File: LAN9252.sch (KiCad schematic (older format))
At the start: 47 parts, among them U1 LAN9252, U2 24LC00, Y1 Crystal_GND24

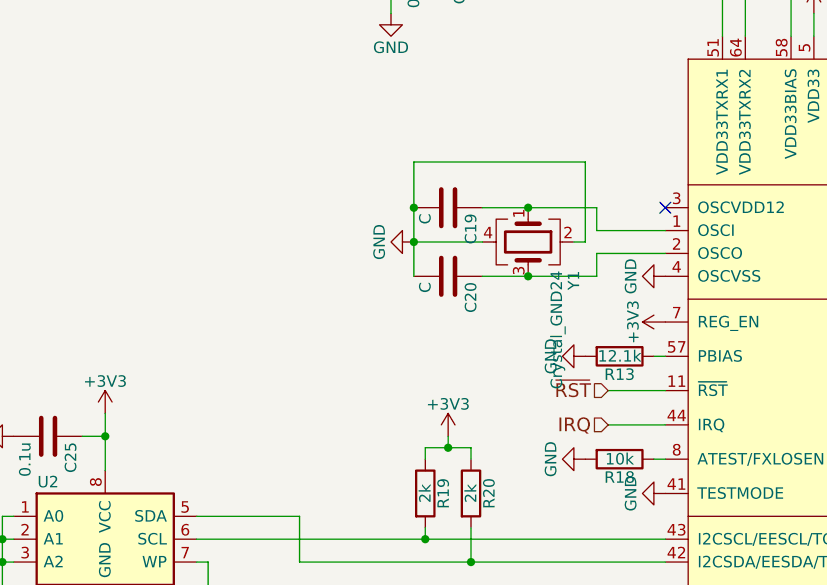
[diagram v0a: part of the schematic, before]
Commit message: 外形線を変更
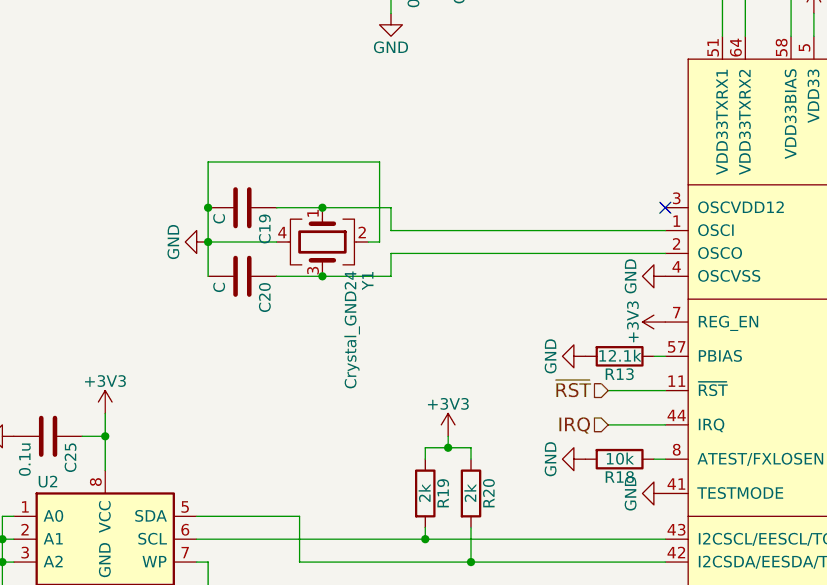
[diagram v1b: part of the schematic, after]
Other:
- moved on the sheet: C19, C20, Y1
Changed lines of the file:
@@
 L C C19
 U 1 1 58DB294F
-P 3650 3850
-F 0 "C19" H 3675 3950 50  0000 L CNN
-F 1 "C" H 3675 3750 50  0000 L CNN
-F 2 "Capacitors_SMD:C_0603" H 3688 3700 50  0001 C CNN
-F 3 "" H 3650 3850 50  0000 C CNN
-	1    3650 3850
+P 2750 3850
+F 0 "C19" H 2775 3950 50  0000 L CNN
+F 1 "C" H 2775 3750 50  0000 L CNN
+F 2 "Capacitors_SMD:C_0603" H 2788 3700 50  0001 C CNN
+F 3 "" H 2750 3850 50  0000 C CNN
+	1    2750 3850
 	0    1    1    0
 $EndComp
@@
 L C C20
 U 1 1 58DB2B1B
-P 3650 4150
-F 0 "C20" H 3675 4250 50  0000 L CNN
-F 1 "C" H 3675 4050 50  0000 L CNN
-F 2 "Capacitors_SMD:C_0603" H 3688 4000 50  0001 C CNN
-F 3 "" H 3650 4150 50  0000 C CNN
-	1    3650 4150
+P 2750 4150
+F 0 "C20" H 2775 4250 50  0000 L CNN
+F 1 "C" H 2775 4050 50  0000 L CNN
+F 2 "Capacitors_SMD:C_0603" H 2788 4000 50  0001 C CNN
+F 3 "" H 2750 4150 50  0000 C CNN
+	1    2750 4150
 	0    1    1    0
 $EndComp
@@
 L GND #PWR055
 U 1 1 58DB2B81
-P 3500 4000
-F 0 "#PWR055" H 3500 3750 50  0001 C CNN
-F 1 "GND" H 3500 3850 50  0000 C CNN
-F 2 "" H 3500 4000 50  0000 C CNN
-F 3 "" H 3500 4000 50  0000 C CNN
-	1    3500 4000
+P 2600 4000
+F 0 "#PWR055" H 2600 3750 50  0001 C CNN
+F 1 "GND" H 2600 3850 50  0000 C CNN
+F 2 "" H 2600 4000 50  0000 C CNN
+F 3 "" H 2600 4000 50  0000 C CNN
+	1    2600 4000
 	0    1    1    0
 $EndComp
@@
 Connection ~ 7150 3450
 Wire Wire Line
-	3500 3650 3500 4150
-Connection ~ 3500 4000
-Wire Wire Line
-	3800 4150 4300 4150
-Wire Wire Line
-	3800 3850 4300 3850
-Wire Wire Line
-	4600 3950 4300 3950
-Wire Wire Line
-	4300 3950 4300 3850
-Connection ~ 4000 3850
-Wire Wire Line
-	4600 4050 4300 4050
-Wire Wire Line
-	4300 4050 4300 4150
-Connection ~ 4000 4150
+	2600 3650 2600 4150
+Connection ~ 2600 4000
+Wire Wire Line
+	2900 4150 3400 4150
+Wire Wire Line
+	2900 3850 3400 3850
+Wire Wire Line
+	3400 3950 4600 3950
+Wire Wire Line
+	3400 3850 3400 3950
+Connection ~ 3100 3850
+Wire Wire Line
+	3400 4050 4600 4050
+Wire Wire Line
+	3400 4050 3400 4150
+Connection ~ 3100 4150
 Wire Wire Line
 	3350 1600 3350 2600
@@
 L Crystal_GND24 Y1
 U 1 1 58DA8433
-P 4000 4000
-F 0 "Y1" H 4125 4200 50  0000 L CNN
-F 1 "Crystal_GND24" H 4125 4125 50  0000 L CNN
-F 2 "Crystals:Crystal_SMD_Abracon_ABM8G-4pin_3.2x2.5mm" H 4000 4000 50  0001 C CNN
-F 3 "" H 4000 4000 50  0001 C CNN
-	1    4000 4000
-	0    1    1    0
-$EndComp
-Wire Wire Line
-	3800 4000 3500 4000
-Wire Wire Line
-	4200 4000 4250 4000
-Wire Wire Line
-	4250 4000 4250 3650
-Wire Wire Line
-	4250 3650 3500 3650
-Connection ~ 3500 3850
+P 3100 4000
+F 0 "Y1" H 3225 4200 50  0000 L CNN
+F 1 "Crystal_GND24" H 3225 4125 50  0000 L CNN
+F 2 "Crystals:Crystal_SMD_Abracon_ABM8G-4pin_3.2x2.5mm" H 3100 4000 50  0001 C CNN
+F 3 "" H 3100 4000 50  0001 C CNN
+	1    3100 4000
+	0    1    1    0
+$EndComp
+Wire Wire Line
+	2900 4000 2600 4000
+Wire Wire Line
+	3300 4000 3350 4000
+Wire Wire Line
+	3350 4000 3350 3650
+Wire Wire Line
+	3350 3650 2600 3650
+Connection ~ 2600 3850
 $Comp
 L LAN9252 U1

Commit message: CHS GNDとPCB GNDを抵抗で接続
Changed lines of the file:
@@
 $EndDescr
 $Comp
-L GND #PWR046
+L GND #PWR050
 U 1 1 58D8F4AE
 P 6400 6000
-F 0 "#PWR046" H 6400 5750 50  0001 C CNN
+F 0 "#PWR050" H 6400 5750 50  0001 C CNN
 F 1 "GND" H 6400 5850 50  0000 C CNN
 F 2 "" H 6400 6000 50  0000 C CNN
@@
 NoConn ~ 4600 3850
 $Comp
-L GND #PWR047
+L GND #PWR051
 U 1 1 58D8FBF8
 P 4600 4150
-F 0 "#PWR047" H 4600 3900 50  0001 C CNN
+F 0 "#PWR051" H 4600 3900 50  0001 C CNN
 F 1 "GND" H 4600 4000 50  0000 C CNN
 F 2 "" H 4600 4150 50  0000 C CNN
@@
 $EndComp
 $Comp
-L GND #PWR048
+L GND #PWR052
 U 1 1 58D8FC8D
 P 4250 4500
-F 0 "#PWR048" H 4250 4250 50  0001 C CNN
+F 0 "#PWR052" H 4250 4250 50  0001 C CNN
 F 1 "GND" H 4250 4350 50  0000 C CNN
 F 2 "" H 4250 4500 50  0000 C CNN
@@
 $EndComp
 $Comp
-L GND #PWR049
+L GND #PWR053
 U 1 1 58D8FD81
 P 4600 5100
-F 0 "#PWR049" H 4600 4850 50  0001 C CNN
+F 0 "#PWR053" H 4600 4850 50  0001 C CNN
 F 1 "GND" H 4600 4950 50  0000 C CNN
 F 2 "" H 4600 5100 50  0000 C CNN
@@
 $EndComp
 $Comp
-L GND #PWR050
+L GND #PWR054
 U 1 1 58D8CF70
 P 7000 3900
-F 0 "#PWR050" H 7000 3650 50  0001 C CNN
+F 0 "#PWR054" H 7000 3650 50  0001 C CNN
 F 1 "GND" H 7000 3750 50  0000 C CNN
 F 2 "" H 7000 3900 50  0000 C CNN
@@
 $EndComp
 $Comp
-L GND #PWR051
+L GND #PWR055
 U 1 1 58D8D10E
 P 7000 5350
-F 0 "#PWR051" H 7000 5100 50  0001 C CNN
+F 0 "#PWR055" H 7000 5100 50  0001 C CNN
 F 1 "GND" H 7000 5200 50  0000 C CNN
 F 2 "" H 7000 5350 50  0000 C CNN
@@
 $EndComp
 $Comp
-L GND #PWR052
+L GND #PWR056
 U 1 1 58D8D588
 P 8150 4700
-F 0 "#PWR052" H 8150 4450 50  0001 C CNN
+F 0 "#PWR056" H 8150 4450 50  0001 C CNN
 F 1 "GND" H 8150 4550 50  0000 C CNN
 F 2 "" H 8150 4700 50  0000 C CNN
@@
 $EndComp
 $Comp
-L GND #PWR053
+L GND #PWR057
 U 1 1 58D8F32E
 P 9350 5550
-F 0 "#PWR053" H 9350 5300 50  0001 C CNN
+F 0 "#PWR057" H 9350 5300 50  0001 C CNN
 F 1 "GND" H 9350 5400 50  0000 C CNN
 F 2 "" H 9350 5550 50  0000 C CNN
@@
 $EndComp
 $Comp
-L GND #PWR054
+L GND #PWR058
 U 1 1 58DAEFCA
 P 7200 3450
-F 0 "#PWR054" H 7200 3200 50  0001 C CNN
+F 0 "#PWR058" H 7200 3200 50  0001 C CNN
 F 1 "GND" H 7200 3300 50  0000 C CNN
 F 2 "" H 7200 3450 50  0000 C CNN
@@
 $EndComp
 $Comp
-L GND #PWR055
+L GND #PWR059
 U 1 1 58DB2B81
 P 2600 4000
-F 0 "#PWR055" H 2600 3750 50  0001 C CNN
+F 0 "#PWR059" H 2600 3750 50  0001 C CNN
 F 1 "GND" H 2600 3850 50  0000 C CNN
 F 2 "" H 2600 4000 50  0000 C CNN
@@
 $EndComp
 $Comp
-L +3V3 #PWR056
+L +3V3 #PWR060
 U 1 1 58DB404A
 P 3350 1600
-F 0 "#PWR056" H 3350 1450 50  0001 C CNN
+F 0 "#PWR060" H 3350 1450 50  0001 C CNN
 F 1 "+3V3" H 3350 1740 50  0000 C CNN
 F 2 "" H 3350 1600 50  0000 C CNN
@@
 $EndComp
 $Comp
-L GND #PWR057
+L GND #PWR061
 U 1 1 58DBACA0
 P 3400 3000
-F 0 "#PWR057" H 3400 2750 50  0001 C CNN
+F 0 "#PWR061" H 3400 2750 50  0001 C CNN
 F 1 "GND" H 3400 2850 50  0000 C CNN
 F 2 "" H 3400 3000 50  0000 C CNN
@@
 $EndComp
 $Comp
-L +3V3 #PWR058
+L +3V3 #PWR062
 U 1 1 58DBB1A4
 P 5250 3000
-F 0 "#PWR058" H 5250 2850 50  0001 C CNN
+F 0 "#PWR062" H 5250 2850 50  0001 C CNN
 F 1 "+3V3" H 5250 3140 50  0000 C CNN
 F 2 "" H 5250 3000 50  0000 C CNN
@@
 $EndComp
 $Comp
-L +3V3 #PWR059
+L +3V3 #PWR063
 U 1 1 58DBB719
 P 5600 3000
-F 0 "#PWR059" H 5600 2850 50  0001 C CNN
+F 0 "#PWR063" H 5600 2850 50  0001 C CNN
 F 1 "+3V3" H 5600 3140 50  0000 C CNN
 F 2 "" H 5600 3000 50  0000 C CNN
@@
 $EndComp
 $Comp
-L +3V3 #PWR060
+L +3V3 #PWR064
 U 1 1 58DBBE53
 P 4600 4350
-F 0 "#PWR060" H 4600 4200 50  0001 C CNN
+F 0 "#PWR064" H 4600 4200 50  0001 C CNN
 F 1 "+3V3" H 4600 4490 50  0000 C CNN
 F 2 "" H 4600 4350 50  0000 C CNN
@@
 $EndComp
 $Comp
-L GND #PWR061
+L GND #PWR065
 U 1 1 58DBE707
 P 7250 2800
-F 0 "#PWR061" H 7250 2550 50  0001 C CNN
+F 0 "#PWR065" H 7250 2550 50  0001 C CNN
 F 1 "GND" H 7250 2650 50  0000 C CNN
 F 2 "" H 7250 2800 50  0000 C CNN
@@
 $EndComp
 $Comp
-L GND #PWR062
+L GND #PWR066
 U 1 1 58DC454A
 P 2300 2450
-F 0 "#PWR062" H 2300 2200 50  0001 C CNN
+F 0 "#PWR066" H 2300 2200 50  0001 C CNN
 F 1 "GND" H 2300 2300 50  0000 C CNN
 F 2 "" H 2300 2450 50  0000 C CNN
@@
 $EndComp
 $Comp
-L +3V3 #PWR063
+L +3V3 #PWR067
 U 1 1 58DC4AF2
 P 2300 1950
-F 0 "#PWR063" H 2300 1800 50  0001 C CNN
+F 0 "#PWR067" H 2300 1800 50  0001 C CNN
 F 1 "+3V3" H 2300 2090 50  0000 C CNN
 F 2 "" H 2300 1950 50  0000 C CNN
@@
 $EndComp
 $Comp
-L GND #PWR064
+L GND #PWR068
 U 1 1 58DD07AD
 P 4250 4950
-F 0 "#PWR064" H 4250 4700 50  0001 C CNN
+F 0 "#PWR068" H 4250 4700 50  0001 C CNN
 F 1 "GND" H 4250 4800 50  0000 C CNN
 F 2 "" H 4250 4950 50  0000 C CNN
@@
 $EndComp
 $Comp
-L +3V3 #PWR065
+L +3V3 #PWR069
 U 1 1 58DD57EA
 P 3650 4850
-F 0 "#PWR065" H 3650 4700 50  0001 C CNN
+F 0 "#PWR069" H 3650 4700 50  0001 C CNN
 F 1 "+3V3" H 3650 4990 50  0000 C CNN
 F 2 "" H 3650 4850 50  0000 C CNN
@@
 	3400 4050 4600 4050
 Wire Wire Line
-	3400 4050 3400 4150
+	3400 4150 3400 4050
 Connection ~ 3100 4150
 Wire Wire Line
@@
 	3000 5200 3000 5400
 $Comp
-L GND #PWR066
+L GND #PWR070
 U 1 1 58E26D3D
 P 2150 5600
-F 0 "#PWR066" H 2150 5350 50  0001 C CNN
+F 0 "#PWR070" H 2150 5350 50  0001 C CNN
 F 1 "GND" H 2150 5450 50  0000 C CNN
 F 2 "" H 2150 5600 50  0000 C CNN
@@
 Connection ~ 1700 5300
 $Comp
-L GND #PWR067
+L GND #PWR071
 U 1 1 58E27E20
 P 1700 5900
-F 0 "#PWR067" H 1700 5650 50  0001 C CNN
+F 0 "#PWR071" H 1700 5650 50  0001 C CNN
 F 1 "GND" H 1700 5750 50  0000 C CNN
 F 2 "" H 1700 5900 50  0000 C CNN
@@
 $EndComp
 $Comp
-L GND #PWR068
+L GND #PWR072
 U 1 1 58E29423
 P 1750 4850
-F 0 "#PWR068" H 1750 4600 50  0001 C CNN
+F 0 "#PWR072" H 1750 4600 50  0001 C CNN
 F 1 "GND" H 1750 4700 50  0000 C CNN
 F 2 "" H 1750 4850 50  0000 C CNN
@@
 $EndComp
 $Comp
-L +3V3 #PWR069
+L +3V3 #PWR073
 U 1 1 58E2970F
 P 2150 4750
-F 0 "#PWR069" H 2150 4600 50  0001 C CNN
+F 0 "#PWR073" H 2150 4600 50  0001 C CNN
 F 1 "+3V3" H 2150 4890 50  0000 C CNN
 F 2 "" H 2150 4750 50  0000 C CNN

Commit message: 抵抗とかコンデンサを追加
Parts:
- added C32, C33: 10u, Capacitors_SMD:C_0805, symbol C
- added R42, R43, R44: 10k, Resistors_SMD:R_0603, symbol R
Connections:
- net +3V3: now also C32.1, C33.1, R42.1
- net GND: now also C32.2, C33.2, R43.2, R44.2
- net LINKACTLED0: now also R43.1
- net LINKACTLED1: now also R44.1
- net RUNLED: now also R42.2
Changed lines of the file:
@@
 $EndDescr
 $Comp
-L GND #PWR050
+L GND #PWR054
 U 1 1 58D8F4AE
 P 6400 6000
-F 0 "#PWR050" H 6400 5750 50  0001 C CNN
+F 0 "#PWR054" H 6400 5750 50  0001 C CNN
 F 1 "GND" H 6400 5850 50  0000 C CNN
 F 2 "" H 6400 6000 50  0000 C CNN
@@
 NoConn ~ 4600 3850
 $Comp
-L GND #PWR051
+L GND #PWR055
 U 1 1 58D8FBF8
 P 4600 4150
-F 0 "#PWR051" H 4600 3900 50  0001 C CNN
+F 0 "#PWR055" H 4600 3900 50  0001 C CNN
 F 1 "GND" H 4600 4000 50  0000 C CNN
 F 2 "" H 4600 4150 50  0000 C CNN
@@
 $EndComp
 $Comp
-L GND #PWR052
+L GND #PWR056
 U 1 1 58D8FC8D
 P 4250 4500
-F 0 "#PWR052" H 4250 4250 50  0001 C CNN
+F 0 "#PWR056" H 4250 4250 50  0001 C CNN
 F 1 "GND" H 4250 4350 50  0000 C CNN
 F 2 "" H 4250 4500 50  0000 C CNN
@@
 $EndComp
 $Comp
-L GND #PWR053
+L GND #PWR057
 U 1 1 58D8FD81
 P 4600 5100
-F 0 "#PWR053" H 4600 4850 50  0001 C CNN
+F 0 "#PWR057" H 4600 4850 50  0001 C CNN
 F 1 "GND" H 4600 4950 50  0000 C CNN
 F 2 "" H 4600 5100 50  0000 C CNN
@@
 $EndComp
 $Comp
-L GND #PWR054
+L GND #PWR058
 U 1 1 58D8CF70
 P 7000 3900
-F 0 "#PWR054" H 7000 3650 50  0001 C CNN
+F 0 "#PWR058" H 7000 3650 50  0001 C CNN
 F 1 "GND" H 7000 3750 50  0000 C CNN
 F 2 "" H 7000 3900 50  0000 C CNN
@@
 $EndComp
 $Comp
-L GND #PWR055
+L GND #PWR059
 U 1 1 58D8D10E
 P 7000 5350
-F 0 "#PWR055" H 7000 5100 50  0001 C CNN
+F 0 "#PWR059" H 7000 5100 50  0001 C CNN
 F 1 "GND" H 7000 5200 50  0000 C CNN
 F 2 "" H 7000 5350 50  0000 C CNN
@@
 $EndComp
 $Comp
-L GND #PWR056
+L GND #PWR060
 U 1 1 58D8D588
 P 8150 4700
-F 0 "#PWR056" H 8150 4450 50  0001 C CNN
+F 0 "#PWR060" H 8150 4450 50  0001 C CNN
 F 1 "GND" H 8150 4550 50  0000 C CNN
 F 2 "" H 8150 4700 50  0000 C CNN
@@
 $EndComp
 $Comp
-L GND #PWR057
+L GND #PWR061
 U 1 1 58D8F32E
 P 9350 5550
-F 0 "#PWR057" H 9350 5300 50  0001 C CNN
+F 0 "#PWR061" H 9350 5300 50  0001 C CNN
 F 1 "GND" H 9350 5400 50  0000 C CNN
 F 2 "" H 9350 5550 50  0000 C CNN
@@
 Text HLabel 9150 4400 2    60   Input ~ 0
 VDDTXRX2
-Text HLabel 4350 5600 0    60   Input ~ 0
+Text HLabel 4050 5600 0    60   Input ~ 0
 LINKACTLED0
-Text HLabel 4350 5700 0    60   Input ~ 0
+Text HLabel 4050 5700 0    60   Input ~ 0
 LINKACTLED1
 $Comp
@@
 $EndComp
 $Comp
-L GND #PWR058
+L GND #PWR062
 U 1 1 58DAEFCA
 P 7200 3450
-F 0 "#PWR058" H 7200 3200 50  0001 C CNN
+F 0 "#PWR062" H 7200 3200 50  0001 C CNN
 F 1 "GND" H 7200 3300 50  0000 C CNN
 F 2 "" H 7200 3450 50  0000 C CNN
@@
 $EndComp
 $Comp
-L GND #PWR059
+L GND #PWR063
 U 1 1 58DB2B81
 P 2600 4000
-F 0 "#PWR059" H 2600 3750 50  0001 C CNN
+F 0 "#PWR063" H 2600 3750 50  0001 C CNN
 F 1 "GND" H 2600 3850 50  0000 C CNN
 F 2 "" H 2600 4000 50  0000 C CNN
@@
 $EndComp
 $Comp
-L +3V3 #PWR060
+L +3V3 #PWR064
 U 1 1 58DB404A
 P 3350 1600
-F 0 "#PWR060" H 3350 1450 50  0001 C CNN
+F 0 "#PWR064" H 3350 1450 50  0001 C CNN
 F 1 "+3V3" H 3350 1740 50  0000 C CNN
 F 2 "" H 3350 1600 50  0000 C CNN
@@
 $EndComp
 $Comp
-L GND #PWR061
+L GND #PWR065
 U 1 1 58DBACA0
 P 3400 3000
-F 0 "#PWR061" H 3400 2750 50  0001 C CNN
+F 0 "#PWR065" H 3400 2750 50  0001 C CNN
 F 1 "GND" H 3400 2850 50  0000 C CNN
 F 2 "" H 3400 3000 50  0000 C CNN
@@
 $EndComp
 $Comp
-L +3V3 #PWR062
+L +3V3 #PWR066
 U 1 1 58DBB1A4
 P 5250 3000
-F 0 "#PWR062" H 5250 2850 50  0001 C CNN
+F 0 "#PWR066" H 5250 2850 50  0001 C CNN
 F 1 "+3V3" H 5250 3140 50  0000 C CNN
 F 2 "" H 5250 3000 50  0000 C CNN
@@
 $EndComp
 $Comp
-L +3V3 #PWR063
+L +3V3 #PWR067
 U 1 1 58DBB719
 P 5600 3000
-F 0 "#PWR063" H 5600 2850 50  0001 C CNN
+F 0 "#PWR067" H 5600 2850 50  0001 C CNN
 F 1 "+3V3" H 5600 3140 50  0000 C CNN
 F 2 "" H 5600 3000 50  0000 C CNN
@@
 $EndComp
 $Comp
-L +3V3 #PWR064
+L +3V3 #PWR068
 U 1 1 58DBBE53
 P 4600 4350
-F 0 "#PWR064" H 4600 4200 50  0001 C CNN
+F 0 "#PWR068" H 4600 4200 50  0001 C CNN
 F 1 "+3V3" H 4600 4490 50  0000 C CNN
 F 2 "" H 4600 4350 50  0000 C CNN
@@
 $EndComp
 $Comp
-L GND #PWR065
+L GND #PWR069
 U 1 1 58DBE707
 P 7250 2800
-F 0 "#PWR065" H 7250 2550 50  0001 C CNN
+F 0 "#PWR069" H 7250 2550 50  0001 C CNN
 F 1 "GND" H 7250 2650 50  0000 C CNN
 F 2 "" H 7250 2800 50  0000 C CNN
@@
 $EndComp
 $Comp
-L GND #PWR066
+L GND #PWR070
 U 1 1 58DC454A
 P 2300 2450
-F 0 "#PWR066" H 2300 2200 50  0001 C CNN
+F 0 "#PWR070" H 2300 2200 50  0001 C CNN
 F 1 "GND" H 2300 2300 50  0000 C CNN
 F 2 "" H 2300 2450 50  0000 C CNN
@@
 $EndComp
 $Comp
-L +3V3 #PWR067
+L +3V3 #PWR071
 U 1 1 58DC4AF2
 P 2300 1950
-F 0 "#PWR067" H 2300 1800 50  0001 C CNN
+F 0 "#PWR071" H 2300 1800 50  0001 C CNN
 F 1 "+3V3" H 2300 2090 50  0000 C CNN
 F 2 "" H 2300 1950 50  0000 C CNN
@@
 $EndComp
 $Comp
-L GND #PWR068
+L GND #PWR072
 U 1 1 58DD07AD
 P 4250 4950
-F 0 "#PWR068" H 4250 4700 50  0001 C CNN
+F 0 "#PWR072" H 4250 4700 50  0001 C CNN
 F 1 "GND" H 4250 4800 50  0000 C CNN
 F 2 "" H 4250 4950 50  0000 C CNN
@@
 $EndComp
 $Comp
-L +3V3 #PWR069
+L +3V3 #PWR073
 U 1 1 58DD57EA
 P 3650 4850
-F 0 "#PWR069" H 3650 4700 50  0001 C CNN
+F 0 "#PWR073" H 3650 4700 50  0001 C CNN
 F 1 "+3V3" H 3650 4990 50  0000 C CNN
 F 2 "" H 3650 4850 50  0000 C CNN
@@
 Connection ~ 6650 2350
 Wire Wire Line
-	1800 2050 1800 2000
-Wire Wire Line
-	1800 2000 2800 2000
+	1800 2000 1800 2050
+Wire Wire Line
+	1300 2000 2800 2000
 Wire Wire Line
 	2800 2000 2800 2050
@@
 	2800 2400 2800 2350
 Wire Wire Line
-	1800 2400 2800 2400
+	1300 2400 2800 2400
 Wire Wire Line
 	1800 2400 1800 2350
@@
 	4600 4800 4350 4800
 Wire Wire Line
-	4350 5600 4600 5600
-Wire Wire Line
-	4350 5700 4600 5700
+	4050 5600 4600 5600
+Wire Wire Line
+	4050 5700 4600 5700
 Wire Wire Line
 	4550 4950 4600 4950
@@
 	3550 4950 3550 4900
 Wire Wire Line
-	3550 4900 3750 4900
+	3250 4900 3750 4900
 Wire Wire Line
 	3750 4900 3750 4950
@@
 	3000 5200 3000 5400
 $Comp
-L GND #PWR070
+L GND #PWR074
 U 1 1 58E26D3D
 P 2150 5600
-F 0 "#PWR070" H 2150 5350 50  0001 C CNN
+F 0 "#PWR074" H 2150 5350 50  0001 C CNN
 F 1 "GND" H 2150 5450 50  0000 C CNN
 F 2 "" H 2150 5600 50  0000 C CNN
@@
 Connection ~ 1700 5300
 $Comp
-L GND #PWR071
+L GND #PWR075
 U 1 1 58E27E20
 P 1700 5900
-F 0 "#PWR071" H 1700 5650 50  0001 C CNN
+F 0 "#PWR075" H 1700 5650 50  0001 C CNN
 F 1 "GND" H 1700 5750 50  0000 C CNN
 F 2 "" H 1700 5900 50  0000 C CNN
@@
 $EndComp
 $Comp
-L GND #PWR072
+L GND #PWR076
 U 1 1 58E29423
 P 1750 4850
-F 0 "#PWR072" H 1750 4600 50  0001 C CNN
+F 0 "#PWR076" H 1750 4600 50  0001 C CNN
 F 1 "GND" H 1750 4700 50  0000 C CNN
 F 2 "" H 1750 4850 50  0000 C CNN
@@
 $EndComp
 $Comp
-L +3V3 #PWR073
+L +3V3 #PWR077
 U 1 1 58E2970F
 P 2150 4750
-F 0 "#PWR073" H 2150 4600 50  0001 C CNN
+F 0 "#PWR077" H 2150 4600 50  0001 C CNN
 F 1 "+3V3" H 2150 4890 50  0000 C CNN
 F 2 "" H 2150 4750 50  0000 C CNN
@@
 Connection ~ 6450 3050
 Connection ~ 6800 3350
-Text HLabel 4350 5800 0    60   Input ~ 0
+Text HLabel 3150 5800 0    60   Input ~ 0
 RUNLED
 Wire Wire Line
-	4600 5800 4350 5800
+	3150 5800 4600 5800
+$Comp
+L C C33
+U 1 1 58E57ACE
+P 1500 2200
+F 0 "C33" H 1525 2300 50  0000 L CNN
+F 1 "10u" H 1525 2100 50  0000 L CNN
+F 2 "Capacitors_SMD:C_0805" H 1538 2050 50  0001 C CNN
+F 3 "" H 1500 2200 50  0001 C CNN
+	1    1500 2200
+	1    0    0    -1
+$EndComp
+$Comp
+L C C32
+U 1 1 58E57B8D
+P 1300 2200
+F 0 "C32" H 1325 2300 50  0000 L CNN
+F 1 "10u" H 1325 2100 50  0000 L CNN
+F 2 "Capacitors_SMD:C_0805" H 1338 2050 50  0001 C CNN
+F 3 "" H 1300 2200 50  0001 C CNN
+	1    1300 2200
+	1    0    0    -1
+$EndComp
+Wire Wire Line
+	1500 2050 1500 2000
+Connection ~ 1800 2000
+Wire Wire Line
+	1300 2050 1300 2000
+Connection ~ 1500 2000
+Wire Wire Line
+	1500 2350 1500 2400
+Connection ~ 1800 2400
+Wire Wire Line
+	1300 2350 1300 2400
+Connection ~ 1500 2400
+$Comp
+L R R42
+U 1 1 58E5AADD
+P 3250 5600
+F 0 "R42" V 3330 5600 50  0000 C CNN
+F 1 "10k" V 3250 5600 50  0000 C CNN
+F 2 "Resistors_SMD:R_0603" V 3180 5600 50  0001 C CNN
+F 3 "" H 3250 5600 50  0001 C CNN
+	1    3250 5600
+	1    0    0    -1
+$EndComp
+Wire Wire Line
+	3250 5750 3250 5800
+Connection ~ 3250 5800
+Wire Wire Line
+	3250 5450 3250 4900
+Connection ~ 3550 4900
+$Comp
+L R R43
+U 1 1 58E5BBE5
+P 4150 6050
+F 0 "R43" V 4230 6050 50  0000 C CNN
+F 1 "10k" V 4150 6050 50  0000 C CNN
+F 2 "Resistors_SMD:R_0603" V 4080 6050 50  0001 C CNN
+F 3 "" H 4150 6050 50  0001 C CNN
+	1    4150 6050
+	1    0    0    -1
+$EndComp
+$Comp
+L R R44
+U 1 1 58E5BCC2
+P 4350 6050
+F 0 "R44" V 4430 6050 50  0000 C CNN
+F 1 "10k" V 4350 6050 50  0000 C CNN
+F 2 "Resistors_SMD:R_0603" V 4280 6050 50  0001 C CNN
+F 3 "" H 4350 6050 50  0001 C CNN
+	1    4350 6050
+	1    0    0    -1
+$EndComp
+Wire Wire Line
+	4150 5900 4150 5600
+Connection ~ 4150 5600
+Wire Wire Line
+	4350 5900 4350 5700
+Connection ~ 4350 5700
+Wire Wire Line
+	4150 6200 4150 6250
+Wire Wire Line
+	4150 6250 4350 6250
+Wire Wire Line
+	4350 6250 4350 6200
+$Comp
+L GND #PWR078
+U 1 1 58E5C0F4
+P 4250 6300
+F 0 "#PWR078" H 4250 6050 50  0001 C CNN
+F 1 "GND" H 4250 6150 50  0000 C CNN
+F 2 "" H 4250 6300 50  0000 C CNN
+F 3 "" H 4250 6300 50  0000 C CNN
+	1    4250 6300
+	1    0    0    -1
+$EndComp
+Wire Wire Line
+	4250 6300 4250 6250
+Connection ~ 4250 6250
 $EndSCHEMATC

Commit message: viaの調整
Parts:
- added R45: 4.7k, Resistors_SMD:R_0603, symbol R
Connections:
- net GND: now also R45.2; no longer U2.1 (A0), U2.2 (A1), U2.3 (A2), U2.7 (WP)
- new net: R45.1, U2.1 (A0), U2.2 (A1), U2.3 (A2), U2.7 (WP)
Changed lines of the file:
@@
 L GND #PWR075
 U 1 1 58E27E20
-P 1700 5900
-F 0 "#PWR075" H 1700 5650 50  0001 C CNN
-F 1 "GND" H 1700 5750 50  0000 C CNN
-F 2 "" H 1700 5900 50  0000 C CNN
-F 3 "" H 1700 5900 50  0000 C CNN
-	1    1700 5900
+P 1700 6200
+F 0 "#PWR075" H 1700 5950 50  0001 C CNN
+F 1 "GND" H 1700 6050 50  0000 C CNN
+F 2 "" H 1700 6200 50  0000 C CNN
+F 3 "" H 1700 6200 50  0000 C CNN
+	1    1700 6200
 	1    0    0    -1
 $EndComp
@@
 	4250 6300 4250 6250
 Connection ~ 4250 6250
+$Comp
+L R R45
+U 1 1 58E6BD7D
+P 1700 6050
+F 0 "R45" V 1780 6050 50  0000 C CNN
+F 1 "4.7k" V 1700 6050 50  0000 C CNN
+F 2 "Resistors_SMD:R_0603" V 1630 6050 50  0001 C CNN
+F 3 "" H 1700 6050 50  0001 C CNN
+	1    1700 6050
+	1    0    0    -1
+$EndComp
 $EndSCHEMATC
